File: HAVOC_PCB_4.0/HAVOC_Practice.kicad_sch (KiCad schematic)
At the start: 43 parts, among them J1 132134, J10 BATT/switch, J3 NG, J7 solenoid, J8 Micro_SD_Card, J9 BNO, Q1 NMOS, Q2 NMOS, Q3 NMOS, Q4 NMOS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

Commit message: wiring new connectors
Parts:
- removed D5: LED_Dual_AAKK, Connector_Molex:Molex_Mini-Fit_Jr_5569-04A2_2x02_P4.20mm_Horizontal, symbol Device:LED_Dual_AAKK
- added D2, D3: LED, Connector_Molex:Molex_Mini-Fit_Jr_5569-02A2_2x01_P4.20mm_Horizontal, symbol Device:LED
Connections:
- net +12V: now also J7.3 (Pin_3); no longer J7.2 (Pin_2)
- net +5V: now also D9.2 (BA), D2.1 (A), D3.1 (A); no longer D9.1 (BA)
- net at Q3.1 (D): now also D9.1 (RK); no longer D9.2 (RK)
- net at Q6.1 (D): now also D2.2 (K), D3.2 (K)
- net at Q1.1 (D): now also J7.2 (Pin_2); no longer J7.3 (Pin_3)
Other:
- moved on the sheet: Q2, R8

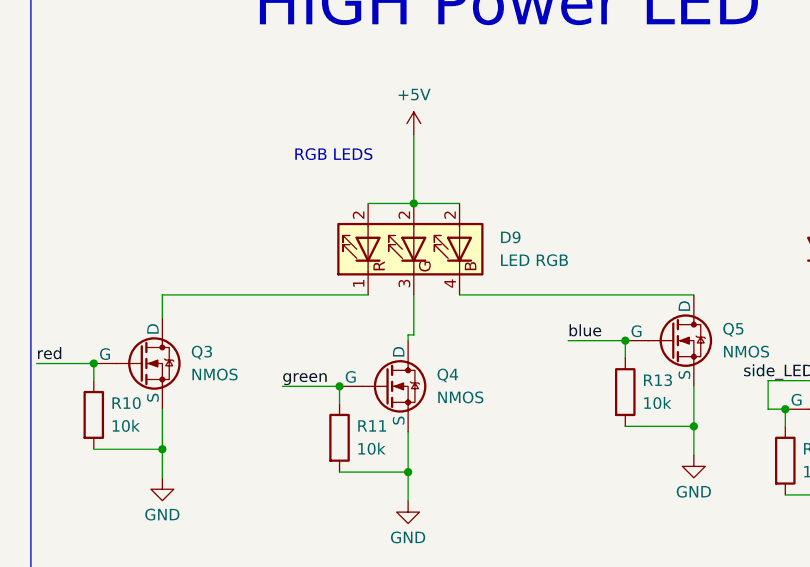
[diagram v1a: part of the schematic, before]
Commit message: adding traces, still needs solenoid traces mich have to change pins
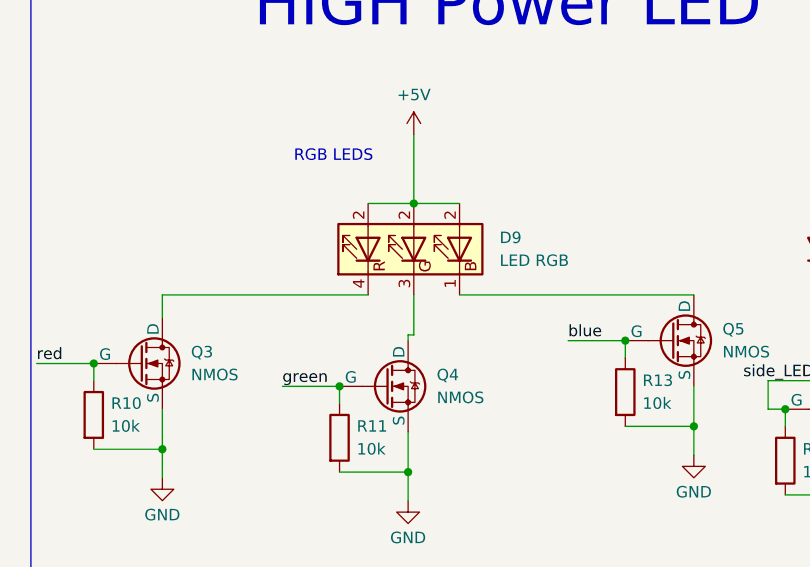
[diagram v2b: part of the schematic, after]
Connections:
- net at Q3.1 (D): now also D9.4 (RK); no longer D9.1 (RK)
- net at Q5.1 (D): now also D9.1 (BK); no longer D9.4 (BK)

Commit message: penis
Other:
- note added: "penis"
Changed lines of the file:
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@@
+		)
+	)
+	(text "penis"
+		(exclude_from_sim no)
+		(at 151.13 205.486 0)
+		(effects
+			(font
+				(size 1.27 1.27)
+			)
 		)
 	)
